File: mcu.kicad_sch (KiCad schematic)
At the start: 17 parts, among them SW301 SW_Push, U301 STM32F103C8Tx, U302 M95640-WMN6TP, Y301 8MHz

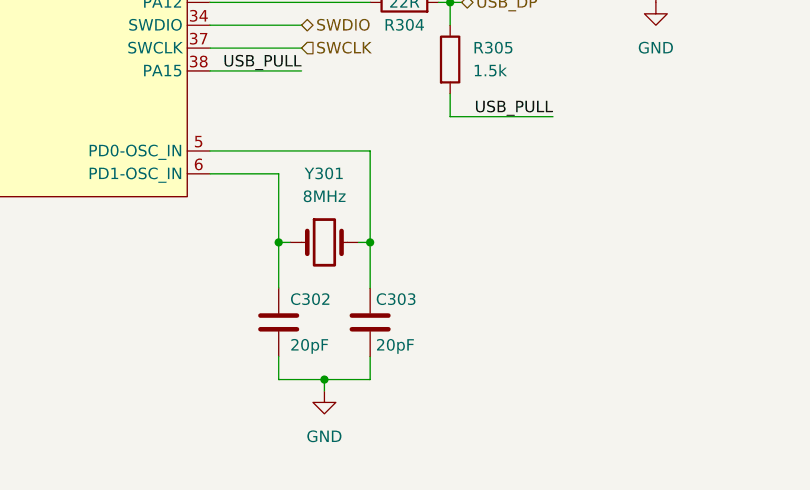
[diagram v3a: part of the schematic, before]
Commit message: Change to smaller 12MHz crystal
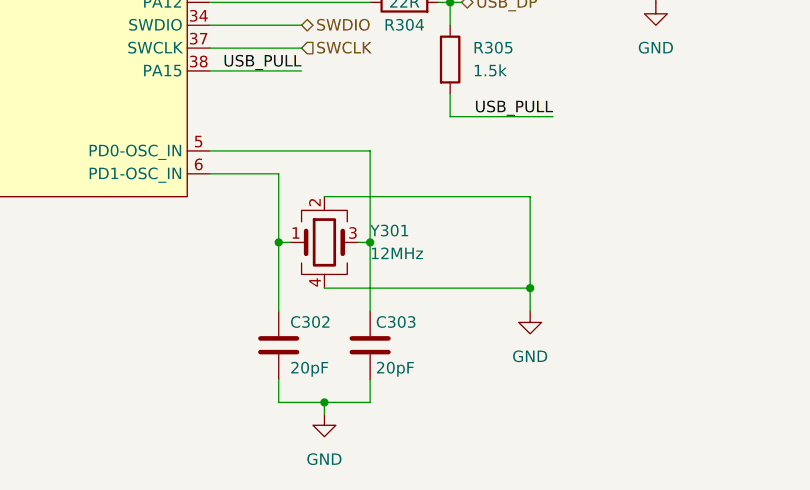
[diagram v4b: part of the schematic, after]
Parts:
- removed Y301: 8MHz, Crystal:Crystal_SMD_HC49-SD_HandSoldering, symbol Device:Crystal
- added Y301: 12MHz, Crystal:Crystal_SMD_3225-4Pin_3.2x2.5mm_HandSoldering, symbol Device:Crystal_GND24
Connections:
- net GND: now also Y301.2, Y301.4
- net at C303.1, U301.5 (PD0-OSC_IN): now also Y301.3
- net at C302.1, U301.6 (PD1-OSC_IN): now also Y301.1
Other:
- moved on the sheet: C302, C303
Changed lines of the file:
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@@
   (junction (at 74.93 50.8) (diameter 0.9144) (color 0 0 0 0))
   (junction (at 134.62 124.46) (diameter 0.9144) (color 0 0 0 0))
-  (junction (at 139.7 139.7) (diameter 0.9144) (color 0 0 0 0))
+  (junction (at 139.7 142.24) (diameter 0.9144) (color 0 0 0 0))
   (junction (at 144.78 124.46) (diameter 0.9144) (color 0 0 0 0))
   (junction (at 153.67 97.79) (diameter 0.9144) (color 0 0 0 0))
+  (junction (at 162.56 129.54) (diameter 0.9144) (color 0 0 0 0))
   (junction (at 176.53 90.17) (diameter 0.9144) (color 0 0 0 0))
   (junction (at 191.77 40.64) (diameter 0.9144) (color 0 0 0 0))
@@
     (stroke (width 0) (type solid) (color 0 0 0 0))
   )
-  (wire (pts (xy 134.62 124.46) (xy 134.62 129.54))
-    (stroke (width 0) (type solid) (color 0 0 0 0))
-  )
-  (wire (pts (xy 134.62 137.16) (xy 134.62 139.7))
-    (stroke (width 0) (type solid) (color 0 0 0 0))
-  )
-  (wire (pts (xy 134.62 139.7) (xy 139.7 139.7))
+  (wire (pts (xy 134.62 124.46) (xy 134.62 132.08))
+    (stroke (width 0) (type solid) (color 0 0 0 0))
+  )
+  (wire (pts (xy 134.62 139.7) (xy 134.62 142.24))
+    (stroke (width 0) (type solid) (color 0 0 0 0))
+  )
+  (wire (pts (xy 134.62 142.24) (xy 139.7 142.24))
     (stroke (width 0) (type solid) (color 0 0 0 0))
   )
@@
     (stroke (width 0) (type solid) (color 0 0 0 0))
   )
-  (wire (pts (xy 139.7 139.7) (xy 139.7 140.97))
+  (wire (pts (xy 139.7 119.38) (xy 162.56 119.38))
+    (stroke (width 0) (type solid) (color 0 0 0 0))
+  )
+  (wire (pts (xy 139.7 129.54) (xy 162.56 129.54))
+    (stroke (width 0) (type solid) (color 0 0 0 0))
+  )
+  (wire (pts (xy 139.7 142.24) (xy 139.7 143.51))
     (stroke (width 0) (type solid) (color 0 0 0 0))
   )
@@
     (stroke (width 0) (type solid) (color 0 0 0 0))
   )
-  (wire (pts (xy 144.78 124.46) (xy 144.78 129.54))
-    (stroke (width 0) (type solid) (color 0 0 0 0))
-  )
-  (wire (pts (xy 144.78 137.16) (xy 144.78 139.7))
-    (stroke (width 0) (type solid) (color 0 0 0 0))
-  )
-  (wire (pts (xy 144.78 139.7) (xy 139.7 139.7))
+  (wire (pts (xy 144.78 124.46) (xy 144.78 132.08))
+    (stroke (width 0) (type solid) (color 0 0 0 0))
+  )
+  (wire (pts (xy 144.78 139.7) (xy 144.78 142.24))
+    (stroke (width 0) (type solid) (color 0 0 0 0))
+  )
+  (wire (pts (xy 144.78 142.24) (xy 139.7 142.24))
     (stroke (width 0) (type solid) (color 0 0 0 0))
   )
@@
   )
   (wire (pts (xy 153.67 110.49) (xy 165.1 110.49))
+    (stroke (width 0) (type solid) (color 0 0 0 0))
+  )
+  (wire (pts (xy 162.56 119.38) (xy 162.56 129.54))
+    (stroke (width 0) (type solid) (color 0 0 0 0))
+  )
+  (wire (pts (xy 162.56 129.54) (xy 162.56 132.08))
     (stroke (width 0) (type solid) (color 0 0 0 0))
   )
@@
     (pin "1")
   )
-  (symbol (lib_id "power:GND") (at 139.7 140.97 0) (unit 1)
-    (in_bom yes) (on_board yes) (fields_autoplaced)
-    (property "Reference" "#PWR0304" (id 0) (at 139.7 147.32 0)
-      (effects (font (size 1.27 1.27)) hide)
-    )
-    (property "Value" "GND" (id 1) (at 139.7 146.05 0))
-    (property "Footprint" "" (id 2) (at 139.7 140.97 0)
-      (effects (font (size 1.27 1.27)) hide)
-    )
-    (property "Datasheet" "" (id 3) (at 139.7 140.97 0)
+  (symbol (lib_id "power:GND") (at 139.7 143.51 0) (unit 1)
+    (in_bom yes) (on_board yes) (fields_autoplaced)
+    (property "Reference" "#PWR0304" (id 0) (at 139.7 149.86 0)
+      (effects (font (size 1.27 1.27)) hide)
+    )
+    (property "Value" "GND" (id 1) (at 139.7 148.59 0))
+    (property "Footprint" "" (id 2) (at 139.7 143.51 0)
+      (effects (font (size 1.27 1.27)) hide)
+    )
+    (property "Datasheet" "" (id 3) (at 139.7 143.51 0)
       (effects (font (size 1.27 1.27)) hide)
     )
@@
     )
     (property "Datasheet" "" (id 3) (at 142.24 58.42 0)
+      (effects (font (size 1.27 1.27)) hide)
+    )
+    (pin "1")
+  )
+  (symbol (lib_id "power:GND") (at 162.56 132.08 0) (unit 1)
+    (in_bom yes) (on_board yes) (fields_autoplaced)
+    (property "Reference" "#PWR0311" (id 0) (at 162.56 138.43 0)
+      (effects (font (size 1.27 1.27)) hide)
+    )
+    (property "Value" "GND" (id 1) (at 162.56 137.16 0))
+    (property "Footprint" "" (id 2) (at 162.56 132.08 0)
+      (effects (font (size 1.27 1.27)) hide)
+    )
+    (property "Datasheet" "" (id 3) (at 162.56 132.08 0)
       (effects (font (size 1.27 1.27)) hide)
     )
@@
     (pin "2")
   )
-  (symbol (lib_id "Device:C") (at 134.62 133.35 0) (unit 1)
-    (in_bom yes) (on_board yes)
-    (property "Reference" "C302" (id 0) (at 135.89 130.8099 0)
-      (effects (font (size 1.27 1.27)) (justify left))
-    )
-    (property "Value" "20pF" (id 1) (at 135.89 135.8899 0)
-      (effects (font (size 1.27 1.27)) (justify left))
-    )
-    (property "Footprint" "Capacitor_SMD:C_0805_2012Metric_Pad1.18x1.45mm_HandSolder" (id 2) (at 135.5852 137.16 0)
-      (effects (font (size 1.27 1.27)) hide)
-    )
-    (property "Datasheet" "~" (id 3) (at 134.62 133.35 0)
-      (effects (font (size 1.27 1.27)) hide)
-    )
-    (pin "1")
-    (pin "2")
-  )
-  (symbol (lib_id "Device:C") (at 144.78 133.35 0) (unit 1)
-    (in_bom yes) (on_board yes)
-    (property "Reference" "C303" (id 0) (at 145.415 130.81 0)
-      (effects (font (size 1.27 1.27)) (justify left))
-    )
-    (property "Value" "20pF" (id 1) (at 145.415 135.89 0)
-      (effects (font (size 1.27 1.27)) (justify left))
-    )
-    (property "Footprint" "Capacitor_SMD:C_0805_2012Metric_Pad1.18x1.45mm_HandSolder" (id 2) (at 145.7452 137.16 0)
-      (effects (font (size 1.27 1.27)) hide)
-    )
-    (property "Datasheet" "~" (id 3) (at 144.78 133.35 0)
+  (symbol (lib_id "Device:C") (at 134.62 135.89 0) (unit 1)
+    (in_bom yes) (on_board yes)
+    (property "Reference" "C302" (id 0) (at 135.89 133.3499 0)
+      (effects (font (size 1.27 1.27)) (justify left))
+    )
+    (property "Value" "20pF" (id 1) (at 135.89 138.4299 0)
+      (effects (font (size 1.27 1.27)) (justify left))
+    )
+    (property "Footprint" "Capacitor_SMD:C_0805_2012Metric_Pad1.18x1.45mm_HandSolder" (id 2) (at 135.5852 139.7 0)
+      (effects (font (size 1.27 1.27)) hide)
+    )
+    (property "Datasheet" "~" (id 3) (at 134.62 135.89 0)
+      (effects (font (size 1.27 1.27)) hide)
+    )
+    (pin "1")
+    (pin "2")
+  )
+  (symbol (lib_id "Device:C") (at 144.78 135.89 0) (unit 1)
+    (in_bom yes) (on_board yes)
+    (property "Reference" "C303" (id 0) (at 145.415 133.35 0)
+      (effects (font (size 1.27 1.27)) (justify left))
+    )
+    (property "Value" "20pF" (id 1) (at 145.415 138.43 0)
+      (effects (font (size 1.27 1.27)) (justify left))
+    )
+    (property "Footprint" "Capacitor_SMD:C_0805_2012Metric_Pad1.18x1.45mm_HandSolder" (id 2) (at 145.7452 139.7 0)
+      (effects (font (size 1.27 1.27)) hide)
+    )
+    (property "Datasheet" "~" (id 3) (at 144.78 135.89 0)
       (effects (font (size 1.27 1.27)) hide)
     )
@@
     (pin "2")
   )
-  (symbol (lib_id "Device:Crystal") (at 139.7 124.46 0) (unit 1)
-    (in_bom yes) (on_board yes) (fields_autoplaced)
-    (property "Reference" "Y301" (id 0) (at 139.7 116.84 0))
-    (property "Value" "8MHz" (id 1) (at 139.7 119.38 0))
-    (property "Footprint" "Crystal:Crystal_SMD_HC49-SD_HandSoldering" (id 2) (at 139.7 124.46 0)
+  (symbol (lib_id "Device:Crystal_GND24") (at 139.7 124.46 0) (unit 1)
+    (in_bom yes) (on_board yes) (fields_autoplaced)
+    (property "Reference" "Y301" (id 0) (at 144.78 123.1899 0)
+      (effects (font (size 1.27 1.27)) (justify left))
+    )
+    (property "Value" "12MHz" (id 1) (at 144.78 125.7299 0)
+      (effects (font (size 1.27 1.27)) (justify left))
+    )
+    (property "Footprint" "Crystal:Crystal_SMD_3225-4Pin_3.2x2.5mm_HandSoldering" (id 2) (at 139.7 124.46 0)
       (effects (font (size 1.27 1.27)) hide)
     )
@@
     (pin "1")
     (pin "2")
+    (pin "3")
+    (pin "4")
   )
   (symbol (lib_id "GozLib:M95640-WMN6TP") (at 209.55 38.1 0) (unit 1)

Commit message: Start PCB
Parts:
- R301, R302, R303, R304, R305, R306, R307, R308, R309: footprint Resistor_SMD:R_0805_2012Metric_Pad1.20x1.40mm_HandSolder -> Resistor_SMD:R_0603_1608Metric_Pad0.98x0.95mm_HandSolder
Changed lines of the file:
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@@
   (symbol (lib_id "power:+3V3") (at 195.58 29.21 0) (unit 1)
     (in_bom yes) (on_board yes) (fields_autoplaced)
-    (property "Reference" "#PWR0307" (id 0) (at 195.58 33.02 0)
+    (property "Reference" "#PWR0308" (id 0) (at 195.58 33.02 0)
       (effects (font (size 1.27 1.27)) hide)
     )
@@
   (symbol (lib_id "power:+3V3") (at 228.6 52.07 0) (unit 1)
     (in_bom yes) (on_board yes) (fields_autoplaced)
-    (property "Reference" "#PWR0309" (id 0) (at 228.6 55.88 0)
+    (property "Reference" "#PWR0310" (id 0) (at 228.6 55.88 0)
       (effects (font (size 1.27 1.27)) hide)
     )
@@
   (symbol (lib_id "power:GND") (at 162.56 132.08 0) (unit 1)
     (in_bom yes) (on_board yes) (fields_autoplaced)
-    (property "Reference" "#PWR0311" (id 0) (at 162.56 138.43 0)
+    (property "Reference" "#PWR0306" (id 0) (at 162.56 138.43 0)
       (effects (font (size 1.27 1.27)) hide)
     )
@@
   (symbol (lib_id "power:GND") (at 176.53 97.79 0) (unit 1)
     (in_bom yes) (on_board yes) (fields_autoplaced)
-    (property "Reference" "#PWR0306" (id 0) (at 176.53 104.14 0)
+    (property "Reference" "#PWR0307" (id 0) (at 176.53 104.14 0)
       (effects (font (size 1.27 1.27)) hide)
     )
@@
   (symbol (lib_id "power:GND") (at 196.85 58.42 0) (unit 1)
     (in_bom yes) (on_board yes) (fields_autoplaced)
-    (property "Reference" "#PWR0308" (id 0) (at 196.85 64.77 0)
+    (property "Reference" "#PWR0309" (id 0) (at 196.85 64.77 0)
       (effects (font (size 1.27 1.27)) hide)
     )
@@
   (symbol (lib_id "power:GND") (at 243.84 49.53 0) (unit 1)
     (in_bom yes) (on_board yes) (fields_autoplaced)
-    (property "Reference" "#PWR0310" (id 0) (at 243.84 55.88 0)
+    (property "Reference" "#PWR0311" (id 0) (at 243.84 55.88 0)
       (effects (font (size 1.27 1.27)) hide)
     )
@@
       (effects (font (size 1.27 1.27)) (justify left))
     )
-    (property "Footprint" "Resistor_SMD:R_0805_2012Metric_Pad1.20x1.40mm_HandSolder" (id 2) (at 73.152 44.45 90)
+    (property "Footprint" "Resistor_SMD:R_0603_1608Metric_Pad0.98x0.95mm_HandSolder" (id 2) (at 73.152 44.45 90)
       (effects (font (size 1.27 1.27)) hide)
     )
@@
     (property "Reference" "R302" (id 0) (at 135.89 53.34 90))
     (property "Value" "10k" (id 1) (at 135.89 55.88 90))
-    (property "Footprint" "Resistor_SMD:R_0805_2012Metric_Pad1.20x1.40mm_HandSolder" (id 2) (at 135.89 57.658 90)
+    (property "Footprint" "Resistor_SMD:R_0603_1608Metric_Pad0.98x0.95mm_HandSolder" (id 2) (at 135.89 57.658 90)
       (effects (font (size 1.27 1.27)) hide)
     )
@@
     (property "Reference" "R303" (id 0) (at 148.59 92.71 90))
     (property "Value" "22R" (id 1) (at 148.59 95.25 90))
-    (property "Footprint" "Resistor_SMD:R_0805_2012Metric_Pad1.20x1.40mm_HandSolder" (id 2) (at 148.59 97.028 90)
+    (property "Footprint" "Resistor_SMD:R_0603_1608Metric_Pad0.98x0.95mm_HandSolder" (id 2) (at 148.59 97.028 90)
       (effects (font (size 1.27 1.27)) hide)
     )
@@
     (property "Reference" "R304" (id 0) (at 148.59 100.33 90))
     (property "Value" "22R" (id 1) (at 148.59 97.79 90))
-    (property "Footprint" "Resistor_SMD:R_0805_2012Metric_Pad1.20x1.40mm_HandSolder" (id 2) (at 148.59 99.568 90)
+    (property "Footprint" "Resistor_SMD:R_0603_1608Metric_Pad0.98x0.95mm_HandSolder" (id 2) (at 148.59 99.568 90)
       (effects (font (size 1.27 1.27)) hide)
     )
@@
       (effects (font (size 1.27 1.27)) (justify left))
     )
-    (property "Footprint" "Resistor_SMD:R_0805_2012Metric_Pad1.20x1.40mm_HandSolder" (id 2) (at 151.892 104.14 90)
+    (property "Footprint" "Resistor_SMD:R_0603_1608Metric_Pad0.98x0.95mm_HandSolder" (id 2) (at 151.892 104.14 90)
       (effects (font (size 1.27 1.27)) hide)
     )
@@
       (effects (font (size 1.27 1.27)) (justify left))
     )
-    (property "Footprint" "Resistor_SMD:R_0805_2012Metric_Pad1.20x1.40mm_HandSolder" (id 2) (at 174.752 93.98 90)
+    (property "Footprint" "Resistor_SMD:R_0603_1608Metric_Pad0.98x0.95mm_HandSolder" (id 2) (at 174.752 93.98 90)
       (effects (font (size 1.27 1.27)) hide)
     )
@@
     (property "Reference" "R307" (id 0) (at 180.34 87.63 90))
     (property "Value" "4.7k" (id 1) (at 180.34 90.17 90))
-    (property "Footprint" "Resistor_SMD:R_0805_2012Metric_Pad1.20x1.40mm_HandSolder" (id 2) (at 180.34 91.948 90)
+    (property "Footprint" "Resistor_SMD:R_0603_1608Metric_Pad0.98x0.95mm_HandSolder" (id 2) (at 180.34 91.948 90)
       (effects (font (size 1.27 1.27)) hide)
     )
@@
       (effects (font (size 1.27 1.27)) (justify left))
     )
-    (property "Footprint" "Resistor_SMD:R_0805_2012Metric_Pad1.20x1.40mm_HandSolder" (id 2) (at 189.992 35.56 90)
+    (property "Footprint" "Resistor_SMD:R_0603_1608Metric_Pad0.98x0.95mm_HandSolder" (id 2) (at 189.992 35.56 90)
       (effects (font (size 1.27 1.27)) hide)
     )
@@
       (effects (font (size 1.27 1.27)) (justify left))
     )
-    (property "Footprint" "Resistor_SMD:R_0805_2012Metric_Pad1.20x1.40mm_HandSolder" (id 2) (at 242.062 45.72 90)
+    (property "Footprint" "Resistor_SMD:R_0603_1608Metric_Pad0.98x0.95mm_HandSolder" (id 2) (at 242.062 45.72 90)
       (effects (font (size 1.27 1.27)) hide)
     )
@@
     (property "Reference" "U301" (id 0) (at 104.14 53.34 0))
     (property "Value" "STM32F103C8Tx" (id 1) (at 104.14 55.88 0))
-    (property "Footprint" "Package_QFP:LQFP-48_7x7mm_P0.5mm" (id 2) (at 91.44 64.77 0)
-      (effects (font (size 1.27 1.27)) hide)
-    )
-    (property "Datasheet" "http://www.st.com/st-web-ui/static/active/en/resource/technical/document/datasheet/CD00161566.pdf" (id 3) (at 91.44 64.77 0)
+    (property "Footprint" "Package_QFP:LQFP-48_7x7mm_P0.5mm" (id 2) (at 74.93 50.8 0)
+      (effects (font (size 1.27 1.27)) hide)
+    )
+    (property "Datasheet" "http://www.st.com/st-web-ui/static/active/en/resource/technical/document/datasheet/CD00161566.pdf" (id 3) (at 107.95 46.99 0)
       (effects (font (size 1.27 1.27)) hide)
     )
@@
     (pin "32")
     (pin "33")
-    (pin "34" (alternate "SWDIO"))
-    (pin "37" (alternate "SWCLK"))
+    (pin "34")
+    (pin "37")
     (pin "38")
     (pin "39")

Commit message: First PCB commit
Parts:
- C301, C302, C303, C304: footprint Capacitor_SMD:C_0805_2012Metric_Pad1.18x1.45mm_HandSolder -> Capacitor_SMD:C_0603_1608Metric_Pad1.08x0.95mm_HandSolder
- renumbered U301 to U203, U302 to U301
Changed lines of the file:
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@@
       (effects (font (size 1.27 1.27)) (justify left))
     )
-    (property "Footprint" "Capacitor_SMD:C_0805_2012Metric_Pad1.18x1.45mm_HandSolder" (id 2) (at 65.7352 58.42 0)
+    (property "Footprint" "Capacitor_SMD:C_0603_1608Metric_Pad1.08x0.95mm_HandSolder" (id 2) (at 65.7352 58.42 0)
       (effects (font (size 1.27 1.27)) hide)
     )
@@
       (effects (font (size 1.27 1.27)) (justify left))
     )
-    (property "Footprint" "Capacitor_SMD:C_0805_2012Metric_Pad1.18x1.45mm_HandSolder" (id 2) (at 135.5852 139.7 0)
+    (property "Footprint" "Capacitor_SMD:C_0603_1608Metric_Pad1.08x0.95mm_HandSolder" (id 2) (at 135.5852 139.7 0)
       (effects (font (size 1.27 1.27)) hide)
     )
@@
       (effects (font (size 1.27 1.27)) (justify left))
     )
-    (property "Footprint" "Capacitor_SMD:C_0805_2012Metric_Pad1.18x1.45mm_HandSolder" (id 2) (at 145.7452 139.7 0)
+    (property "Footprint" "Capacitor_SMD:C_0603_1608Metric_Pad1.08x0.95mm_HandSolder" (id 2) (at 145.7452 139.7 0)
       (effects (font (size 1.27 1.27)) hide)
     )
@@
     (property "Reference" "C304" (id 0) (at 209.55 60.96 90))
     (property "Value" "100nF" (id 1) (at 209.55 58.42 90))
-    (property "Footprint" "Capacitor_SMD:C_0805_2012Metric_Pad1.18x1.45mm_HandSolder" (id 2) (at 205.74 55.5752 0)
+    (property "Footprint" "Capacitor_SMD:C_0603_1608Metric_Pad1.08x0.95mm_HandSolder" (id 2) (at 205.74 55.5752 0)
       (effects (font (size 1.27 1.27)) hide)
     )
@@
   (symbol (lib_id "GozLib:M95640-WMN6TP") (at 209.55 38.1 0) (unit 1)
     (in_bom yes) (on_board yes) (fields_autoplaced)
-    (property "Reference" "U302" (id 0) (at 209.55 27.94 0))
+    (property "Reference" "U301" (id 0) (at 209.55 27.94 0))
     (property "Value" "M95640-WMN6TP" (id 1) (at 209.55 30.48 0))
     (property "Footprint" "Package_SO:SOIC-8_3.9x4.9mm_P1.27mm" (id 2) (at 207.01 19.05 0)
@@
   (symbol (lib_id "GozLib:STM32F103C8Tx") (at 104.14 68.58 0) (unit 1)
     (in_bom yes) (on_board yes) (fields_autoplaced)
-    (property "Reference" "U301" (id 0) (at 104.14 53.34 0))
+    (property "Reference" "U203" (id 0) (at 104.14 53.34 0))
     (property "Value" "STM32F103C8Tx" (id 1) (at 104.14 55.88 0))
     (property "Footprint" "Package_QFP:LQFP-48_7x7mm_P0.5mm" (id 2) (at 74.93 50.8 0)

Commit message: Finish regulator layout
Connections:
- net DIRECTION1: now also U203.21 (PB10); no longer U203.10 (PA0-WKUP)
- net DIRECTION2: now also U203.22 (PB11); no longer U203.11 (PA1)
- net ENABLE_LEFT: now also U203.11 (PA1); no longer U203.21 (PB10)
- net ENABLE_RIGHT: now also U203.10 (PA0-WKUP); no longer U203.22 (PB11)
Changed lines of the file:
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@@
     (effects (font (size 1.27 1.27)) (justify right))
   )
-  (hierarchical_label "ENABLE_LEFT" (shape output) (at 72.39 92.71 180)
+  (hierarchical_label "DIRECTION1" (shape output) (at 72.39 92.71 180)
     (effects (font (size 1.27 1.27)) (justify right))
   )
-  (hierarchical_label "ENABLE_RIGHT" (shape output) (at 72.39 95.25 180)
+  (hierarchical_label "DIRECTION2" (shape output) (at 72.39 95.25 180)
     (effects (font (size 1.27 1.27)) (justify right))
   )
@@
     (effects (font (size 1.27 1.27)) (justify left))
   )
-  (hierarchical_label "DIRECTION1" (shape output) (at 135.89 67.31 0)
+  (hierarchical_label "ENABLE_RIGHT" (shape output) (at 135.89 67.31 0)
     (effects (font (size 1.27 1.27)) (justify left))
   )
-  (hierarchical_label "DIRECTION2" (shape output) (at 135.89 69.85 0)
+  (hierarchical_label "ENABLE_LEFT" (shape output) (at 135.89 69.85 0)
     (effects (font (size 1.27 1.27)) (justify left))
   )
